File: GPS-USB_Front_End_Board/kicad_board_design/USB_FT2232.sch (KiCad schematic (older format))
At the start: 52 parts, among them J1 Micro-USB Connector, U1 93LCxxB, U2 FT2232HL-REEL, U3 L4931 LDO, U8 LT1719S6 -- Not Populated, Y1 12MHz Crystal

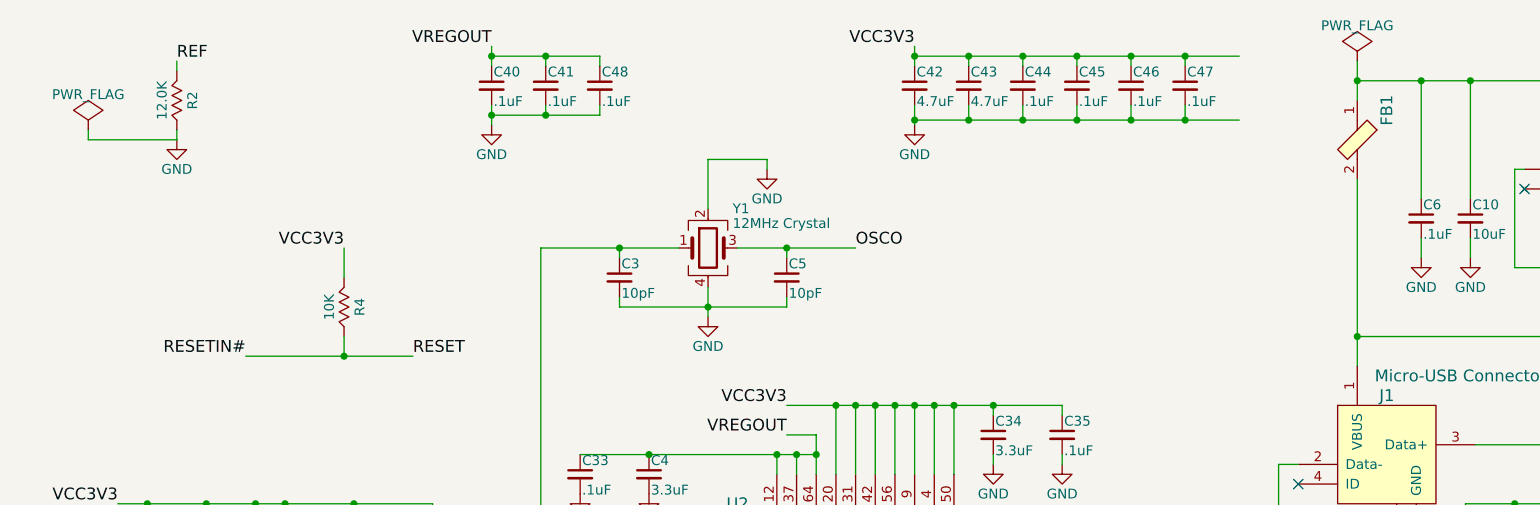
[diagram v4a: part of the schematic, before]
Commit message: Plotted gerbers.  Fixed crystal load caps, added LED, added stitching.
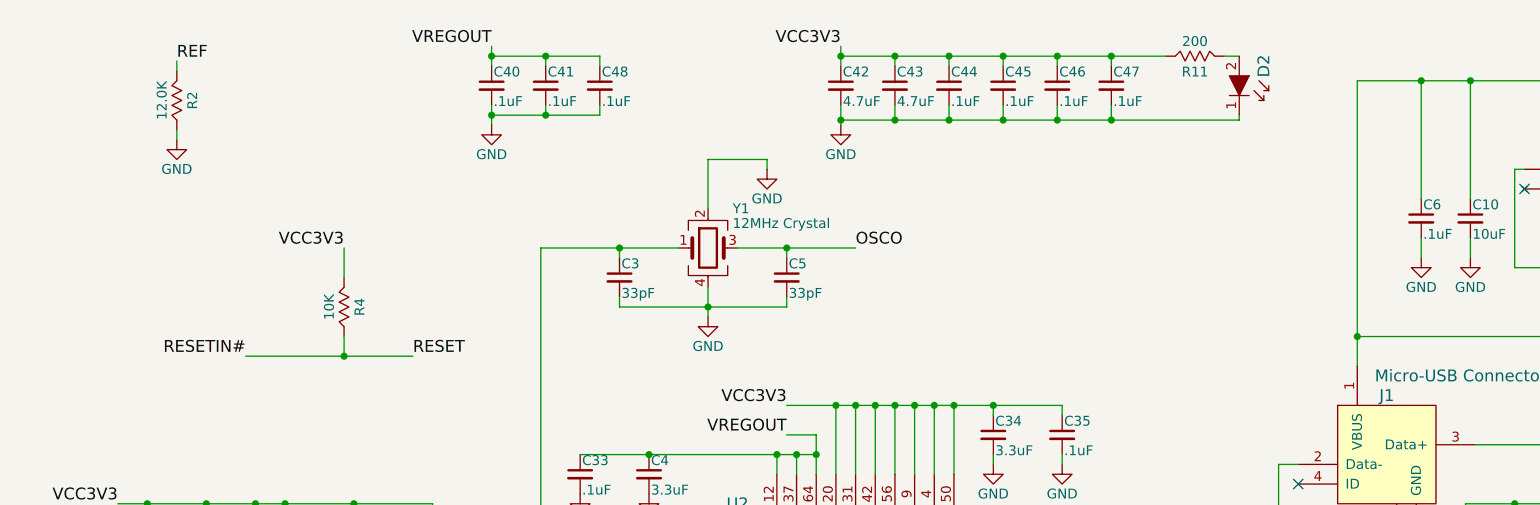
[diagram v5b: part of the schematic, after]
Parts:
- removed FB1: BLM18PG471SN1D, digikey-footprints:0603, symbol BLM18PG471SN1D
- added D2: LTST-C171KRKT, digikey-footprints:0805, symbol LTST-C171KRKT
- added R11: 200, digikey-footprints:0805, symbol R
- C3, C5: value 10pF -> 33pF; MPN C0805C100K5RAC7800 -> C0805C330J5GACTU; SPN 399-17612-1-ND -> 399-1115-1-ND
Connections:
- net VBUS is gone; now on net +5V: C8.1, D1.5, J1.1 (VBUS), TP4.1
- net GND: now also D2.1
- net VCC3V3: now also R11.2
- new net: D2.2, R11.1
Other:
- moved on the sheet: C42, C43, C44, C45, C46, C47

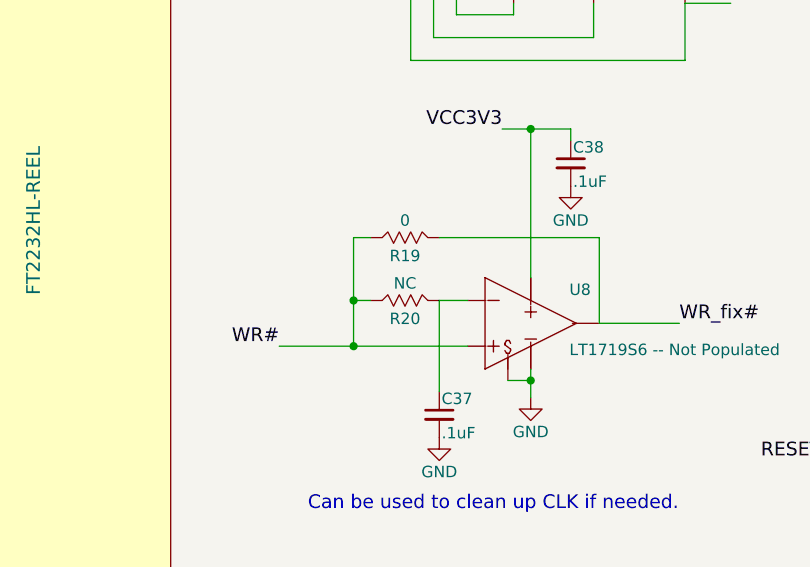
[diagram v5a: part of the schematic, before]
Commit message: Add signals to header.
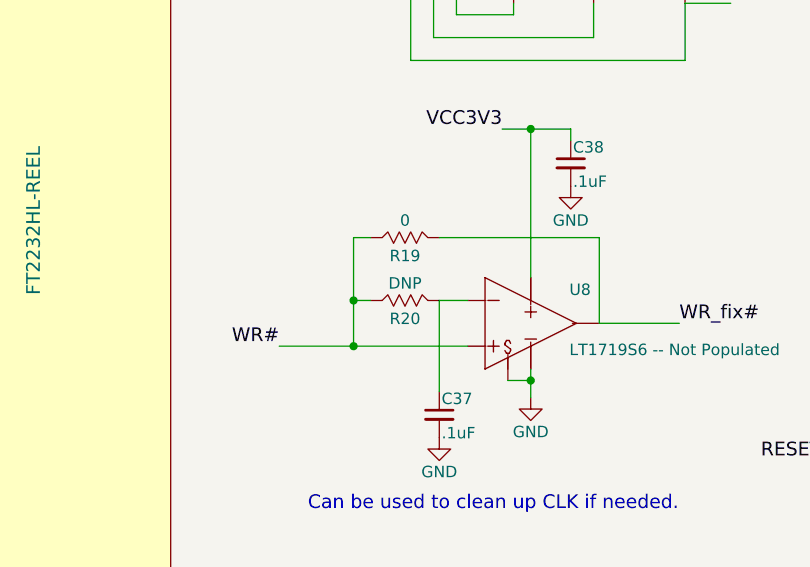
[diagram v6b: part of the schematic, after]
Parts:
- R20: value NC -> DNP
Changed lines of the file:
@@
 P 6475 5450
 F 0 "R20" V 6555 5450 50  0000 C CNN
-F 1 "NC" V 6400 5450 50  0000 C CNN
+F 1 "DNP" V 6400 5450 50  0000 C CNN
 F 2 "Resistors_SMD:R_0603_HandSoldering" V 6330 5450 50  0001 C CNN
 F 3 "" H 6400 5450 50  0001 C CNN

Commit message: Add LED P/N.  Process BOM prior to order.
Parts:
- D2: MFR (none) -> Lite-On; SPN (none) -> 160-1427-1-ND; SPR (none) -> Digikey; SPURL (none) -> -
